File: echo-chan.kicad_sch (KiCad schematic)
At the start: 54 parts, among them J1 SJ1-3533NS, J2 USB_B, SW1 SW_Push, T1 Transformer_1P_1S, U1 JAMMA, U2 JAMMA, U3 AT90USB1286, U4 HD15, U5 AD8054, Y1 16MHz

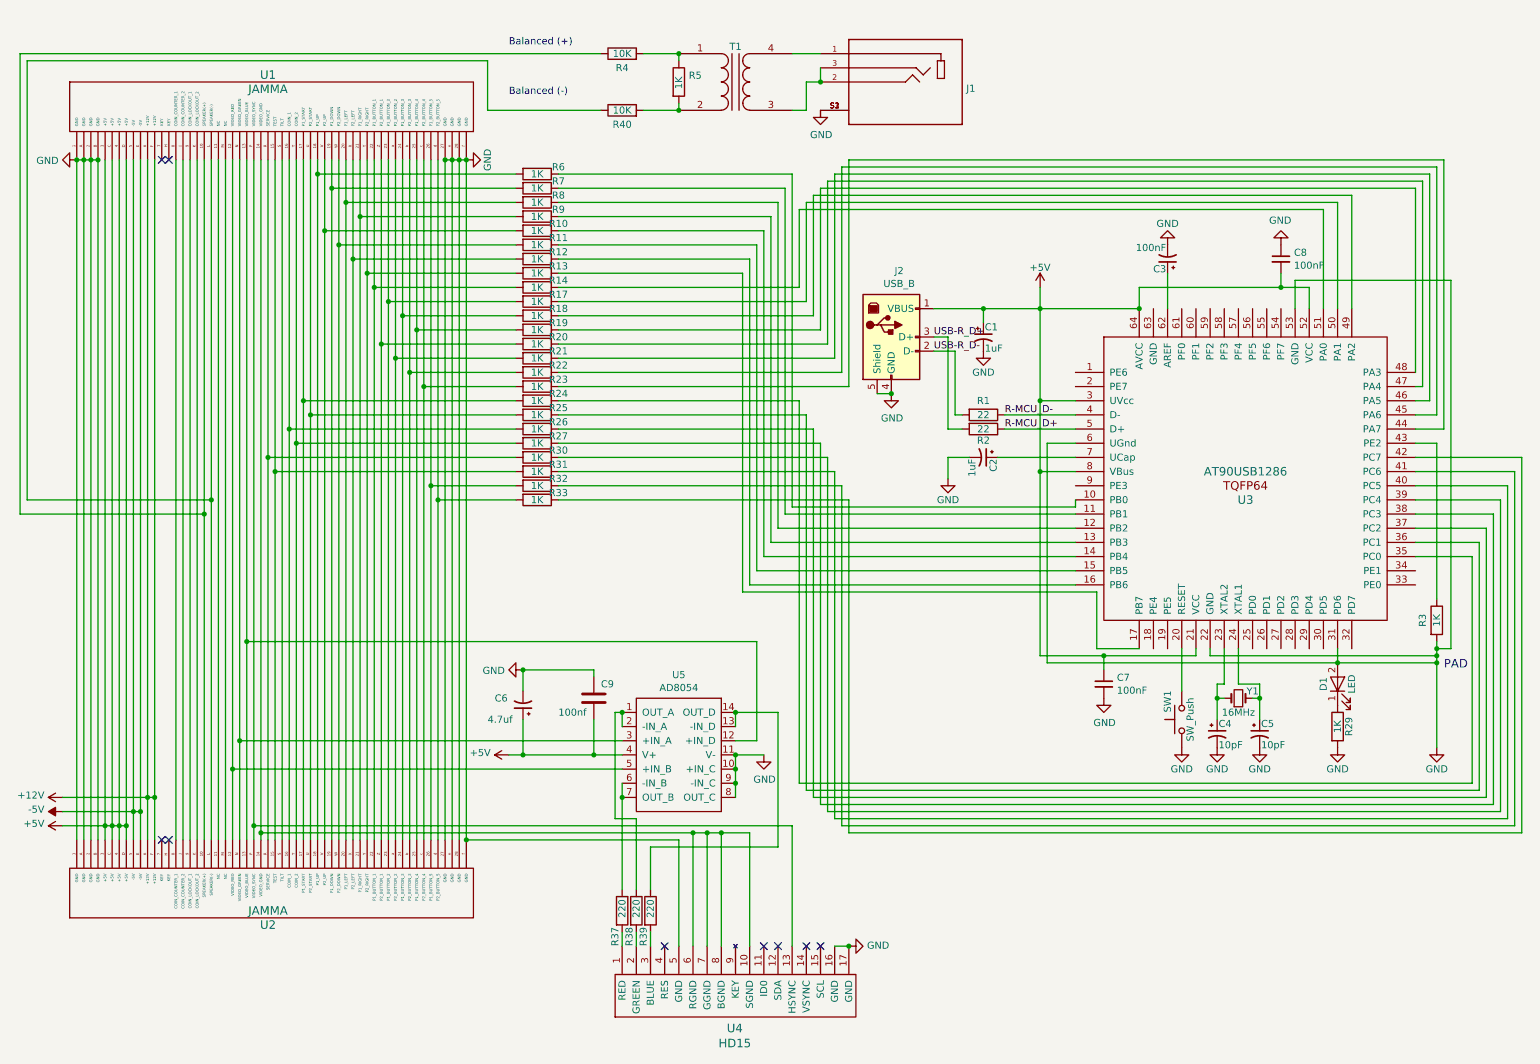
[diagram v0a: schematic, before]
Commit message: Schematic cleanup
- separate +5V and GND lines for readability
- remove useless resistors on MCU input lines
- remove LED
- Add NC sympbols to unused MCU pins
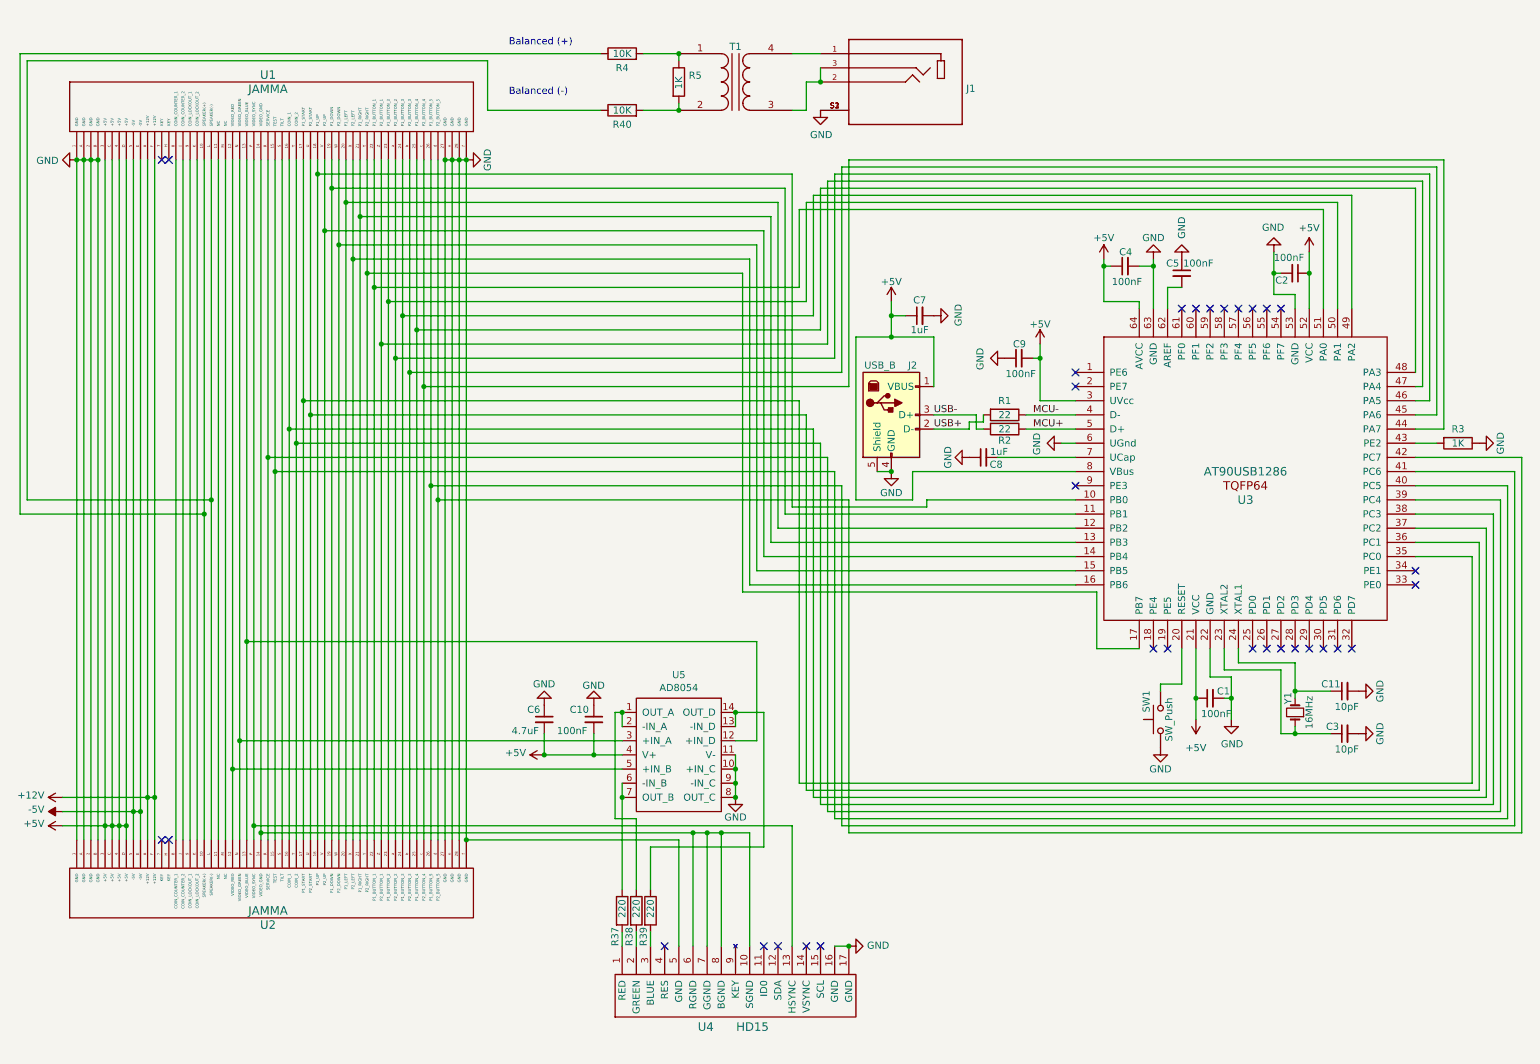
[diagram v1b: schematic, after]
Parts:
- removed C1, C2: 1uF, footprints:C_0603_1608Metric, symbol jamma-streamer-rescue:CP1_Small-jamma-streamer-rescue
- removed C3: 100nF, footprints:C_0603_1608Metric, symbol jamma-streamer-rescue:CP1_Small-jamma-streamer-rescue
- removed C4, C5: 10pF, footprints:C_0603_1608Metric, symbol jamma-streamer-rescue:CP1_Small-jamma-streamer-rescue
- removed C6: 4.7uf, footprints:C_1206_3216Metric_Pad1.42x1.75mm_HandSolder, symbol jamma-streamer-rescue:CP1_Small-Device
- removed C9: 100nf, footprints:C_0603_1608Metric, symbol Device:C
- removed D1: LED, footprints:LED_0603_1608Metric, symbol jamma-streamer-rescue:LED-jamma-streamer-rescue
- removed R10, R11, R12, R13, R14, R17, R18, R19, R20, R21, R22, R23, R24, R25, R26, R27, R30, R31, R32, R33, R6, R7, R8, R9: 1K, footprints:R_0805_2012Metric, symbol Device:R
- removed R29: 1K, footprints:R_0805_2012Metric, symbol jamma-streamer-rescue:R-jamma-streamer-rescue
- added C1, C2, C4, C5, C9: 100nF, Capacitor_SMD:C_0805_2012Metric, symbol Device:C_Small
- added C10: 100nF, symbol Device:C_Small
- added C11, C3: 10pF, symbol Device:C_Small
- added C6: 4.7uF, symbol Device:C_Small
- C7: value 100nF -> 1uF; footprint footprints:C_0603_1608Metric -> Capacitor_SMD:C_0805_2012Metric
- C8: value 100nF -> 1uF; footprint footprints:C_0603_1608Metric -> (none)
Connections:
- net +5V: now also C1.1, C10.2, C2.1, C4.1, C6.2, C9.2; no longer C8.2
- net GND: now also R3.1, U3.63 (GND), C1.2, C10.1, C11.2, C2.2, C3.2, C4.2, C5.1, C6.1, C9.1; no longer R3.2, U3.31 (PD6)
- net at U3.10 (PB0): now also U1.18 (P1_UP), U2.18 (P1_UP)
- net at U3.11 (PB1): now also U1.19 (P1_DOWN), U2.19 (P1_DOWN)
- net at U3.12 (PB2): now also U1.20 (P1_LEFT), U2.20 (P1_LEFT)
- net at U3.13 (PB3): now also U1.21 (P1_RIGHT), U2.21 (P1_RIGHT)
- net at U3.14 (PB4): now also U1.V (P2_UP), U2.V (P2_UP)
- net at U3.15 (PB5): now also U1.W (P2_DOWN), U2.W (P2_DOWN)
- net at U3.16 (PB6): now also U1.X (P2_LEFT), U2.X (P2_LEFT)
- net at U3.17 (PB7): now also U1.Y (P2_RIGHT), U2.Y (P2_RIGHT)
- net at U3.23 (XTAL2), Y1.1: now also C3.1
- net at U3.24 (XTAL1), Y1.2: now also C11.1
- net at U3.35 (PC0): now also U1.17 (P1_START), U2.17 (P1_START)
- net at U3.36 (PC1): now also U1.U (P2_START), U2.U (P2_START)
- net at U3.37 (PC2): now also U1.16 (COIN_1), U2.16 (COIN_1)
- net at U3.38 (PC3): now also U1.T (COIN_2), U2.T (COIN_2)
- net at U3.39 (PC4): now also U1.R (SERVICE), U2.R (SERVICE)
- net at U3.40 (PC5): now also U1.15 (TEST), U2.15 (TEST)
- net at U3.41 (PC6): now also U1.26 (P1_BUTTON_5), U2.26 (P1_BUTTON_5)
- net at U3.42 (PC7): now also U1.d (P2_BUTTON_5), U2.d (P2_BUTTON_5)
- net at U3.43 (PE2): now also R3.2; no longer R3.1
- net at U3.44 (PA7): now also U1.c (P2_BUTTON_4), U2.c (P2_BUTTON_4)
- net at U3.45 (PA6): now also U1.b (P2_BUTTON_3), U2.b (P2_BUTTON_3)
- net at U3.46 (PA5): now also U1.a (P2_BUTTON_2), U2.a (P2_BUTTON_2)
- net at U3.47 (PA4): now also U1.Z (P2_BUTTON_1), U2.Z (P2_BUTTON_1)
- net at U3.48 (PA3): now also U1.25 (P1_BUTTON_4), U2.25 (P1_BUTTON_4)
- net at U3.49 (PA2): now also U1.24 (P1_BUTTON_3), U2.24 (P1_BUTTON_3)
- net at U3.50 (PA1): now also U1.23 (P1_BUTTON_2), U2.23 (P1_BUTTON_2)
- net at U3.51 (PA0): now also U1.22 (P1_BUTTON_1), U2.22 (P1_BUTTON_1)
- net at U3.62 (AREF): now also C5.2
- net at U3.7 (UCap): now also C8.2
- net R-MCU_D+ renamed MCU+
- net R-MCU_D- renamed MCU-
- net USB-R_D+ renamed USB-
- net USB-R_D- renamed USB+
- no-connect marks 9 -> 32
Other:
- note removed: "PAD"
- moved on the sheet: J2, R1, R2, R3, SW1, Y1

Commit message: [SCHEMATIC] Major schematic overhaul
- Replace rats nest of wires with labels
- Separate schematic into sections
- Replace AD8054 with THS7374
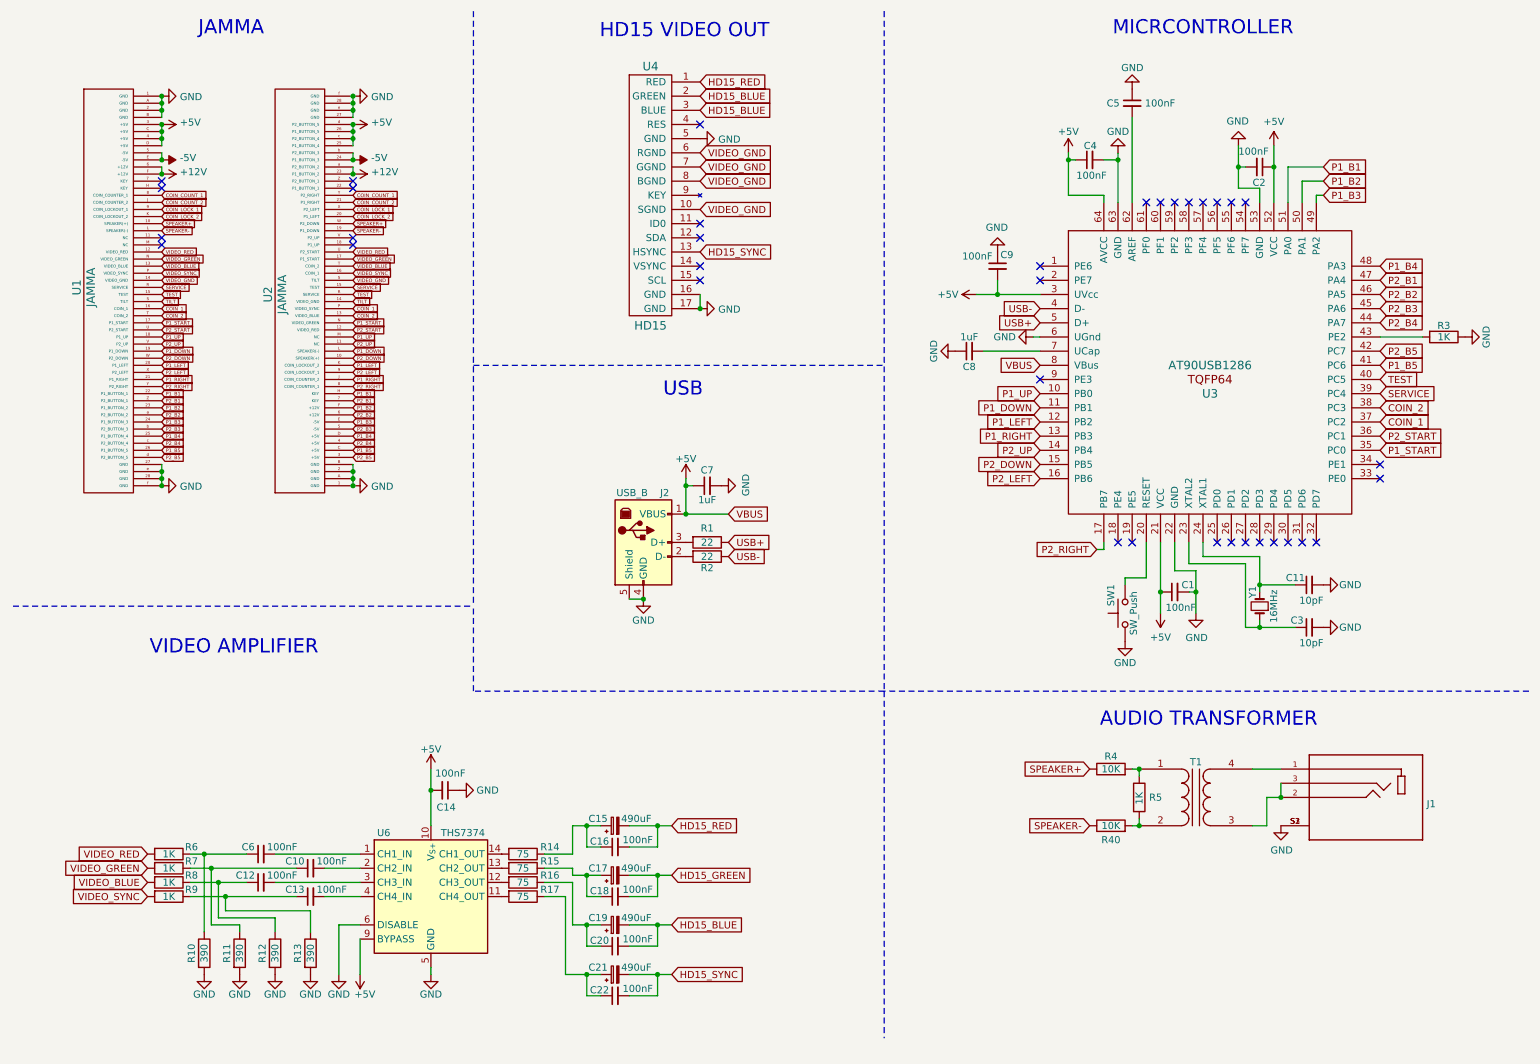
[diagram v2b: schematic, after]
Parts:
- removed R37, R38, R39: 220, footprints:R_0805_2012Metric, symbol Device:R
- removed U5: AD8054, footprints:AD8054ARZ-REEL7, symbol jamma-streamer-rescue:AD8054-jamma
- added C12, C13, C14, C16, C18, C20, C22: 100nF, Capacitor_SMD:C_0805_2012Metric, symbol Device:C_Small
- added C15, C17, C19, C21: 490uF, symbol Device:C_Polarized_Small
- added R10, R11, R12, R13: 390, footprints:R_0805_2012Metric, symbol jamma-streamer-rescue:R-jamma-streamer-rescue
- added R14, R15, R16, R17: 75, footprints:R_0805_2012Metric, symbol jamma-streamer-rescue:R-jamma-streamer-rescue
- added R6, R7, R8, R9: 1K, footprints:R_0805_2012Metric, symbol jamma-streamer-rescue:R-jamma-streamer-rescue
- added U6: THS7374, Package_SO:TSSOP-14_4.4x5mm_P0.65mm, symbol Amplifier_Video:THS7374
- C10: footprint (none) -> Capacitor_SMD:C_0805_2012Metric
- C6: value 4.7uF -> 100nF; footprint (none) -> Capacitor_SMD:C_0805_2012Metric
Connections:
- net +12V: now also U2.23 (P1_BUTTON_2), U2.a (P2_BUTTON_2); no longer U2.6 (+12V), U2.F (+12V)
- net +5V: now also U2.25 (P1_BUTTON_4), U2.26 (P1_BUTTON_5), U2.c (P2_BUTTON_4), U2.d (P2_BUTTON_5), C14.2, U6.10 (V_{S+}), U6.9 (BYPASS); no longer C10.2, C6.2, U2.3 (+5V), U2.4 (+5V), U2.C (+5V), U2.D (+5V)
- net -5V: now also U2.24 (P1_BUTTON_3), U2.b (P2_BUTTON_3); no longer U2.5 (-5V), U2.E (-5V)
- net GND: now also C14.1, R10.2, R11.2, R12.2, R13.2, U6.5 (GND), U6.6 (DISABLE); no longer C10.1, C6.1
- net USB+: now also R1.1, U3.5 (D+); no longer J2.2 (D-), R1.2
- net USB-: now also R2.1, U3.4 (D-); no longer J2.3 (D+), R2.2
- net P1_UP: now reaches U1.18 (P1_UP), U3.10 (PB0)
- net P1_UP: now also U2.M (NC); no longer U2.18 (P1_UP)
- net P1_DOWN: now reaches U1.19 (P1_DOWN), U3.11 (PB1)
- net P1_DOWN: now also U2.L (SPEAKER(-)); no longer U2.19 (P1_DOWN)
- net P1_LEFT: now reaches U1.20 (P1_LEFT), U3.12 (PB2)
- net P1_LEFT: now also U2.K (COIN_LOCKOUT_2); no longer U2.20 (P1_LEFT)
- net P1_RIGHT: now reaches U1.21 (P1_RIGHT), U3.13 (PB3)
- net P1_RIGHT: now also U2.J (COIN_COUNTER_2); no longer U2.21 (P1_RIGHT)
- net P2_UP: now reaches U1.V (P2_UP), U3.14 (PB4)
- net P2_UP: now also U2.11 (NC); no longer U2.V (P2_UP)
- net P2_DOWN: now reaches U1.W (P2_DOWN), U3.15 (PB5)
- net P2_DOWN: now also U2.10 (SPEAKER(+)); no longer U2.W (P2_DOWN)
- net P2_LEFT: now reaches U1.X (P2_LEFT), U3.16 (PB6)
- net P2_LEFT: now also U2.9 (COIN_LOCKOUT_1); no longer U2.X (P2_LEFT)
- net P2_RIGHT: now reaches U1.Y (P2_RIGHT), U3.17 (PB7)
- net P2_RIGHT: now also U2.8 (COIN_COUNTER_1); no longer U2.Y (P2_RIGHT)
- net P1_START: now reaches U1.17 (P1_START), U3.35 (PC0)
- net P1_START: now also U2.N (VIDEO_GREEN); no longer U2.17 (P1_START)
- net P2_START: now reaches U1.U (P2_START), U3.36 (PC1)
- net P2_START: now also U2.12 (VIDEO_RED); no longer U2.U (P2_START)
- net COIN_1: now reaches U1.16 (COIN_1), U3.37 (PC2)
- net COIN_1: now also U2.P (VIDEO_SYNC); no longer U2.16 (COIN_1)
- net COIN_2: now reaches U1.T (COIN_2), U3.38 (PC3)
- net COIN_2: now also U2.13 (VIDEO_BLUE); no longer U2.T (COIN_2)
- net SERVICE: now reaches U1.R (SERVICE), U3.39 (PC4)
- net SERVICE: now also U2.15 (TEST); no longer U2.R (SERVICE)
- net TEST: now reaches U1.15 (TEST), U3.40 (PC5)
- net TEST: now also U2.R (SERVICE); no longer U2.15 (TEST)
- net P1_B5: now reaches U1.26 (P1_BUTTON_5), U3.41 (PC6)
- net P1_B5: now also U2.C (+5V); no longer U2.26 (P1_BUTTON_5)
- net P2_B5: now reaches U1.d (P2_BUTTON_5), U3.42 (PC7)
- net P2_B5: now also U2.3 (+5V); no longer U2.d (P2_BUTTON_5)
- net P2_B4: now reaches U1.c (P2_BUTTON_4), U3.44 (PA7)
- net P2_B4: now also U2.4 (+5V); no longer U2.c (P2_BUTTON_4)
- net P2_B3: now reaches U1.b (P2_BUTTON_3), U3.45 (PA6)
- net P2_B3: now also U2.5 (-5V); no longer U2.b (P2_BUTTON_3)
- net P2_B2: now reaches U1.a (P2_BUTTON_2), U3.46 (PA5)
- net P2_B2: now also U2.6 (+12V); no longer U2.a (P2_BUTTON_2)
- net P2_B1: now reaches U1.Z (P2_BUTTON_1), U3.47 (PA4)
- net P2_B1: now also U2.7 (KEY); no longer U2.Z (P2_BUTTON_1)
- net P1_B4: now reaches U1.25 (P1_BUTTON_4), U3.48 (PA3)
- net P1_B4: now also U2.D (+5V); no longer U2.25 (P1_BUTTON_4)
- net P1_B3: now reaches U1.24 (P1_BUTTON_3), U3.49 (PA2)
- net P1_B3: now also U2.E (-5V); no longer U2.24 (P1_BUTTON_3)
- net P1_B2: now reaches U1.23 (P1_BUTTON_2), U3.50 (PA1)
- net P1_B2: now also U2.F (+12V); no longer U2.23 (P1_BUTTON_2)
- net P1_B1: now reaches U1.22 (P1_BUTTON_1), U3.51 (PA0)
- net P1_B1: now also U2.H (KEY); no longer U2.22 (P1_BUTTON_1)
- net SPEAKER+: now reaches R4.1, U1.10 (SPEAKER(+))
- net SPEAKER+: now also U2.W (P2_DOWN); no longer U2.10 (SPEAKER(+))
- net at U1.11 (NC): no longer U2.11 (NC)
- net VIDEO_RED: now reaches U1.12 (VIDEO_RED)
- net VIDEO_RED: now also U2.U (P2_START), R6.2; no longer U2.12 (VIDEO_RED)
- net VIDEO_BLUE: now reaches U1.13 (VIDEO_BLUE)
- net VIDEO_BLUE: now also U2.T (COIN_2), R8.2; no longer U2.13 (VIDEO_BLUE)
- net VIDEO_GND: now reaches U1.14 (VIDEO_GND), U4.10 (SGND), U4.6 (RGND), U4.7 (GGND), U4.8 (BGND)
- net VIDEO_GND: now also U2.S (TILT); no longer U2.14 (VIDEO_GND)
- net COIN_COUNT_1: now reaches U1.8 (COIN_COUNTER_1)
- net COIN_COUNT_1: now also U2.Y (P2_RIGHT); no longer U2.8 (COIN_COUNTER_1)
- net COIN_LOCK_1: now reaches U1.9 (COIN_LOCKOUT_1)
- net COIN_LOCK_1: now also U2.X (P2_LEFT); no longer U2.9 (COIN_LOCKOUT_1)
- net COIN_COUNT_2: now reaches U1.J (COIN_COUNTER_2)
- net COIN_COUNT_2: now also U2.21 (P1_RIGHT); no longer U2.J (COIN_COUNTER_2)
- net COIN_LOCK_2: now reaches U1.K (COIN_LOCKOUT_2)
- net COIN_LOCK_2: now also U2.20 (P1_LEFT); no longer U2.K (COIN_LOCKOUT_2)
- net SPEAKER-: now reaches R40.1, U1.L (SPEAKER(-))
- net SPEAKER-: now also U2.19 (P1_DOWN); no longer U2.L (SPEAKER(-))
- net at U1.M (NC): no longer U2.M (NC)
- net VIDEO_GREEN: now reaches U1.N (VIDEO_GREEN)
- net VIDEO_GREEN: now also U2.17 (P1_START), R7.2; no longer U2.N (VIDEO_GREEN)
- net TILT: now reaches U1.S (TILT)
- net TILT: now also U2.14 (VIDEO_GND); no longer U2.S (TILT)
- net HD15_RED: now reaches U4.1 (RED)
- net HD15_RED: now also C15.2, C16.2
- net HD15_BLUE: now reaches U4.2 (GREEN)
- net HD15_BLUE: now also U4.3 (BLUE), C19.2, C20.2
- removed net MCU+: R2.1, U3.5 (D+)
- removed net MCU-: R1.1, U3.4 (D-)
- new net: J2.3 (D+), R1.2
- new net: J2.2 (D-), R2.2
- new net: C19.1, C20.1, R16.1
- new net: C21.1, C22.1, R17.1
- new net: C15.1, C16.1, R14.1
- new net: C6.1, R10.1, R6.1
- new net: C10.1, R11.1, R7.1
- new net: C10.2, U6.2 (CH2_IN)
- new net: C12.1, R12.1, R8.1
- new net: C12.2, U6.3 (CH3_IN)
- new net: C6.2, U6.1 (CH1_IN)
- new net: R17.2, U6.11 (CH4_OUT)
- new net: R16.2, U6.12 (CH3_OUT)
- new net: R15.2, U6.13 (CH2_OUT)
- new net: R14.2, U6.14 (CH1_OUT)
- new net: C13.2, U6.4 (CH4_IN)
- new net: C17.1, C18.1, R15.1
- new net: C13.1, R13.1, R9.1
- new net HD15_GREEN: C17.2, C18.2
- new net HD15_SYNC: C21.2, C22.2, U4.13 (HSYNC)
- new net VIDEO_SYNC: R9.2, U1.P (VIDEO_SYNC), U2.16 (COIN_1)
- no-connect marks 32 -> 36
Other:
- note added: "AUDIO TRANSFORMER"
- note added: "HD15 VIDEO OUT"
- note added: "JAMMA"
- note added: "MICRCONTROLLER"
- note added: "USB"
- note added: "VIDEO AMPLIFIER"
- note removed: "Balanced (+)"
- note removed: "Balanced (-)"
- moved on the sheet: C1, C11, C2, C3, C4, C5, C7, C8, C9, J1, J2, R1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
